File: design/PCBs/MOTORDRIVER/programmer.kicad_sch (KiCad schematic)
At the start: 0 parts

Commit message: added programmer
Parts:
- added C13: C, symbol Device:C
- added U2: ATSAMD11D14A-M, Package_DFN_QFN:QFN-24-1EP_4x4mm_P0.5mm_EP2.6x2.6mm, symbol MCU_Microchip_SAMD:ATSAMD11D14A-M

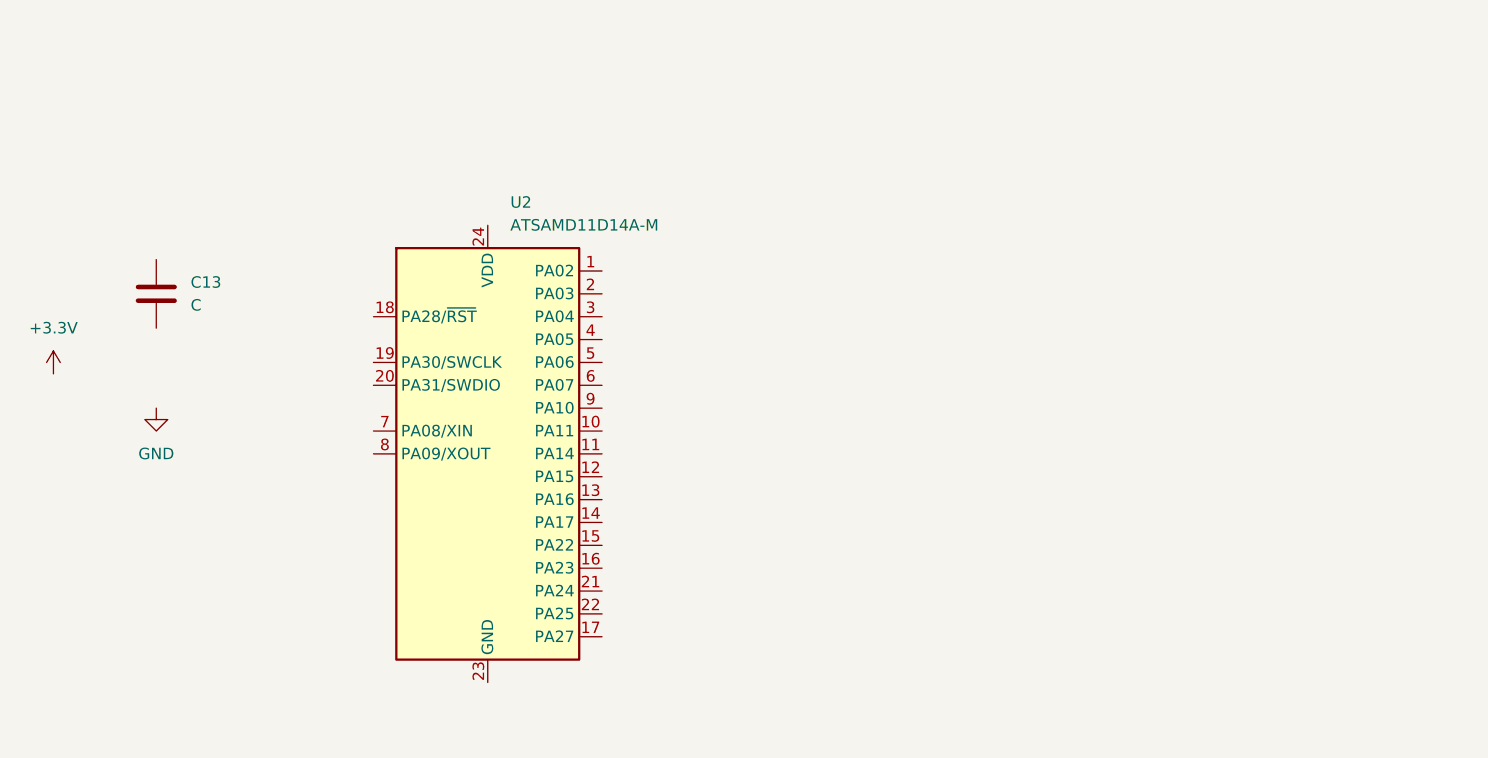
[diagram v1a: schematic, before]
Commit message: USB-C schematics to programmer, programmer to cortex-4 added
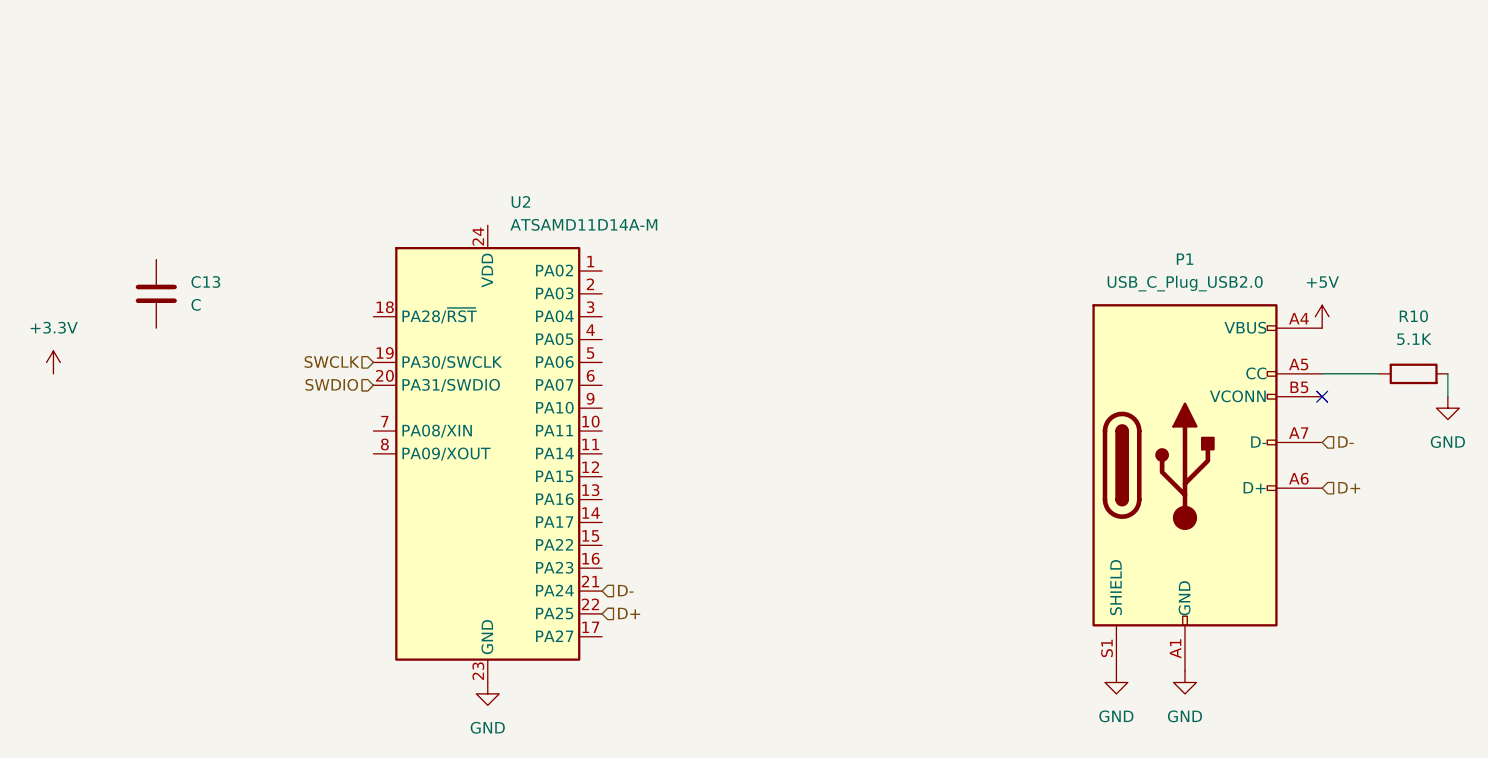
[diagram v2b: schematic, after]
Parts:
- added P1: USB_C_Plug_USB2.0, symbol Connector:USB_C_Plug_USB2.0
- added R10: 5.1K, symbol Device:R
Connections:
- net GND: now also U2.23 (GND), P1.A1 (GND), P1.A12 (GND), P1.B1 (GND), P1.B12 (GND), P1.S1 (SHIELD), R10.2
- net SWCLK: now reaches U2.19 (PA30/SWCLK)
- net SWDIO: now reaches U2.20 (PA31/SWDIO)
- net D-: now reaches U2.21 (PA24)
- net D-: now also P1.A7 (D-)
- net D+: now reaches U2.22 (PA25)
- net D+: now also P1.A6 (D+)
- new net: P1.A5 (CC), R10.1
- new net +5V: P1.A4 (VBUS), P1.A9 (VBUS), P1.B4 (VBUS), P1.B9 (VBUS)
- no-connect marks 0 -> 1

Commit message: First draft of programmer added. GPIO pins are axed atm but can be included if we want some extra functionality, like indicator LEDs or similar.
Routing from USB-C to programmer to main cortex are added. Also
added some datasheets and sources.
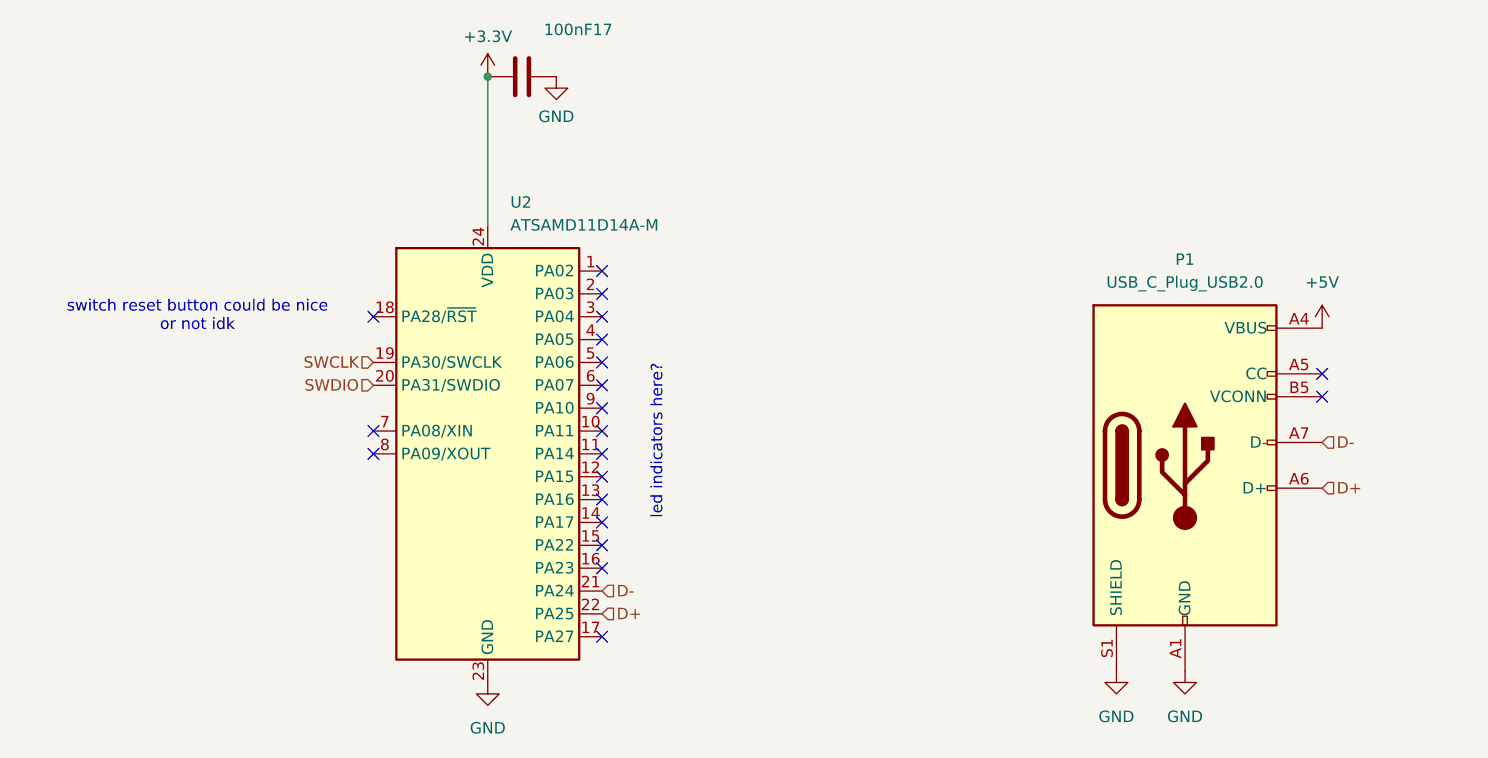
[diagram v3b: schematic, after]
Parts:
- removed C13: C, symbol Device:C
- removed R10: 5.1K, symbol Device:R
- added 100nF17: C, symbol Device:C
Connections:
- net +3.3V: now also U2.24 (VDD), 100nF17.2
- net GND: now also 100nF17.1
- no-connect marks 1 -> 20
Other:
- note added: "led indicators here?"
- note added: "switch reset button could be nice or not idk"

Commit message: fixed schematic layout and added shunt resistor and zener diodes for motor stage
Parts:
- removed P1: USB_C_Plug_USB2.0, symbol Connector:USB_C_Plug_USB2.0
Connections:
- no-connect marks 20 -> 18
